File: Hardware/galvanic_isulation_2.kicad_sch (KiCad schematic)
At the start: 14 parts

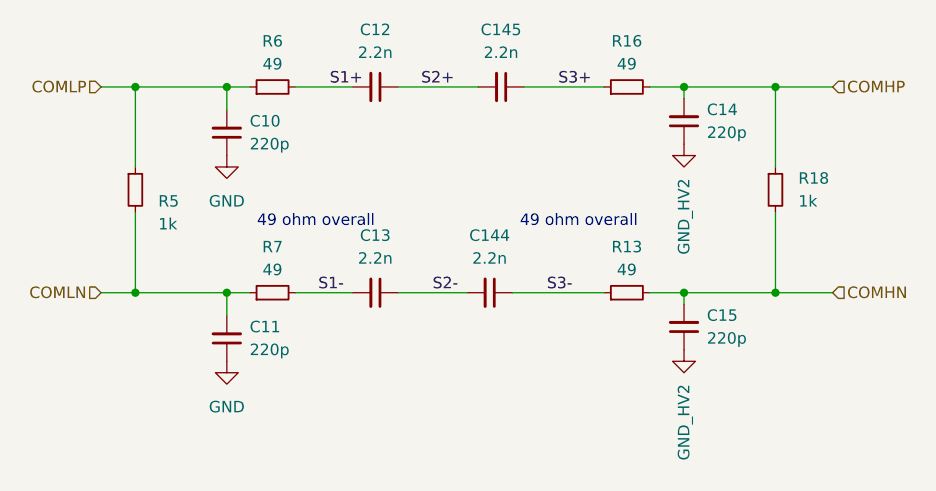
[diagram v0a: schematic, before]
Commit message: Zmiany wizualne w schemacie
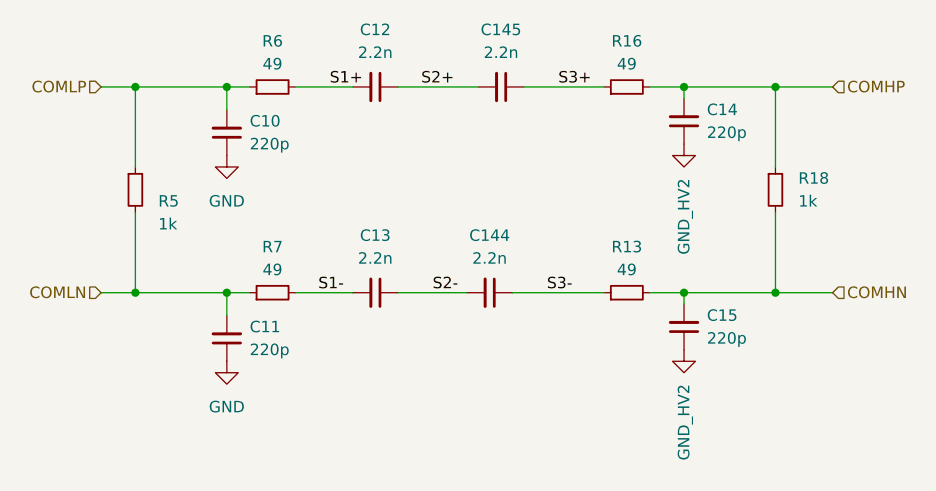
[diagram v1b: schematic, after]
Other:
- note removed: "49 ohm overall"
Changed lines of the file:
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@@
 	(generator_version "9.0")
 	(paper "A4")
-	(text "49 ohm overall\n"
-		(exclude_from_sim no)
-		(at 138.176 97.536 0)
-		(effects
-			(font
-				(size 1.27 1.27)
-			)
-		)
-	)
-	(text "49 ohm overall\n"
-		(exclude_from_sim no)
-		(at 108.966 97.536 0)
-		(effects
-			(font
-				(size 1.27 1.27)
-			)
-		)
-	)
 	(junction
 		(at 149.86 82.55)
